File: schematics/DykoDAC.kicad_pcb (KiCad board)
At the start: 2 copper layers, 159.8 x 100.1 mm, 124 parts, among them J1 AC Input, J2 AudioJack3, J3 USB_B, J4 OLED, J5 Debug, J6 Conn_01x02_Male, SW1 PEC09-2120K, U10 TPA6120, U11 IP4234CZ6, U12 ATSAMD21G18A-AUT, U2 L7809, U3 L7909, U4 L7805, U5 78L05, U8 CS4398, U9 AD8620, X1 22.5792Mhz, X2 24.576Mhz

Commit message: pcb dev.
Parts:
- added D3: LED, LEDs:LED_1206, F.Cu at (50.4, -1.77)
- added R39: 680, Resistors_SMD:R_1206, F.Cu at (49.9, 1.39)
- added U6: LP5907-3.3, TO_SOT_Packages_SMD:SOT-23-5, F.Cu at (115.6, 58.2)
- added U7: LP5907-3.3, TO_SOT_Packages_SMD:SOT-23-5, F.Cu at (65.1, 0.81)
- C2, C3: footprint Capacitors_ThroughHole:CP_Radial_D5.0mm_P2.50mm -> kamtar:CP_Radial_D16.0mm_P7.50mm_Hor
- moved U10 186.8 mm to (137.7, 130.9)
- moved U9 183.6 mm to (116.0, 129.3), turned to 270 degrees
- moved U3 160.0 mm to (91.9, 78.1), turned to 180 degrees
- moved U5 154.2 mm to (120.1, 94.7), turned to 180 degrees
- moved U12 149.8 mm to (78.4, 128.0), turned to 180 degrees
- moved C8 149.3 mm to (98.6, 88.5)
- moved U8 146.4 mm to (98.9, 105.3), turned to 180 degrees
- moved R31 137.7 mm to (64.5, 121.0), turned to 180 degrees
- moved U11 136.7 mm to (63.0, 124.6), turned to 90 degrees
- moved R32 132.4 mm to (64.5, 118.6), turned to 180 degrees
- moved U4 126.3 mm to (95.1, 55.0), turned to 180 degrees
- moved C7 124.8 mm to (94.9, 66.2), turned to 90 degrees
- moved C5 122.9 mm to (90.7, 85.7), turned to 180 degrees
- moved C20 119.8 mm to (118.1, 61.5)
- moved C11 118.7 mm to (101.9, 78.1), turned to 90 degrees
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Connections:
- U11 pad 3: (no net) -> /DykoDAC_MCU/USB_D+
- U11 pad 4: Net-(J3-Pad3) -> /DykoDAC_MCU/USB_D-
- U11 pad 6: /DykoDAC_MCU/USB_D- -> Net-(J3-Pad3)
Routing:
- net /DykoDAC_MCU/VBUS_3V3: track 0.00 -> 15.9 mm
- net /DykoDAC_MCU/USB_D-: track 0.00 -> 12.5 mm
- net /DykoDAC_MCU/USB_D+: track 0.00 -> 11.8 mm
- net Net-(J3-Pad1): track 0.00 -> 9.39 mm, vias 0 -> 2
- net VS_NEG: track 0.00 -> 9.18 mm
- net Net-(J3-Pad3): track 0.00 -> 7.38 mm
- net Net-(J3-Pad2): track 0.00 -> 6.13 mm
- net GND: vias 0 -> 54
- added copper zone on F.Cu, net +3V3
- added copper zone on F.Cu, net +9V
- added copper zone on F.Cu, net -9V
- added copper zone on F.Cu, net GND
- added copper zone on F.Cu, net Net-(C14-Pad1)
- added copper zone on F.Cu, net VS_NEG
- removed copper zone on B.Cu, net GND

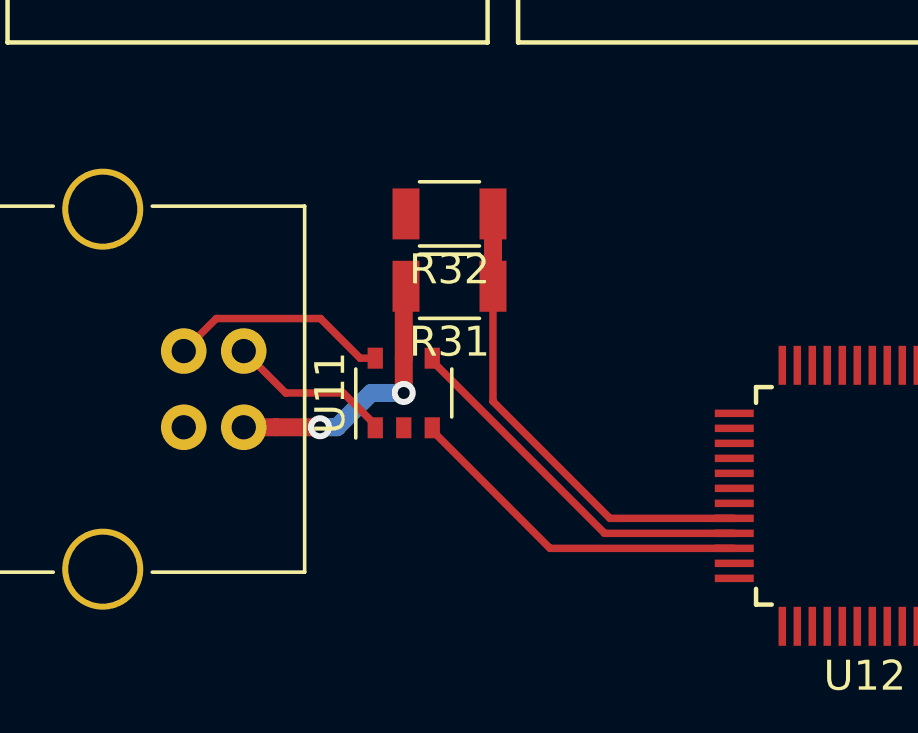
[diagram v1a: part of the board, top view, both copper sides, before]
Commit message: changed usb protection IC
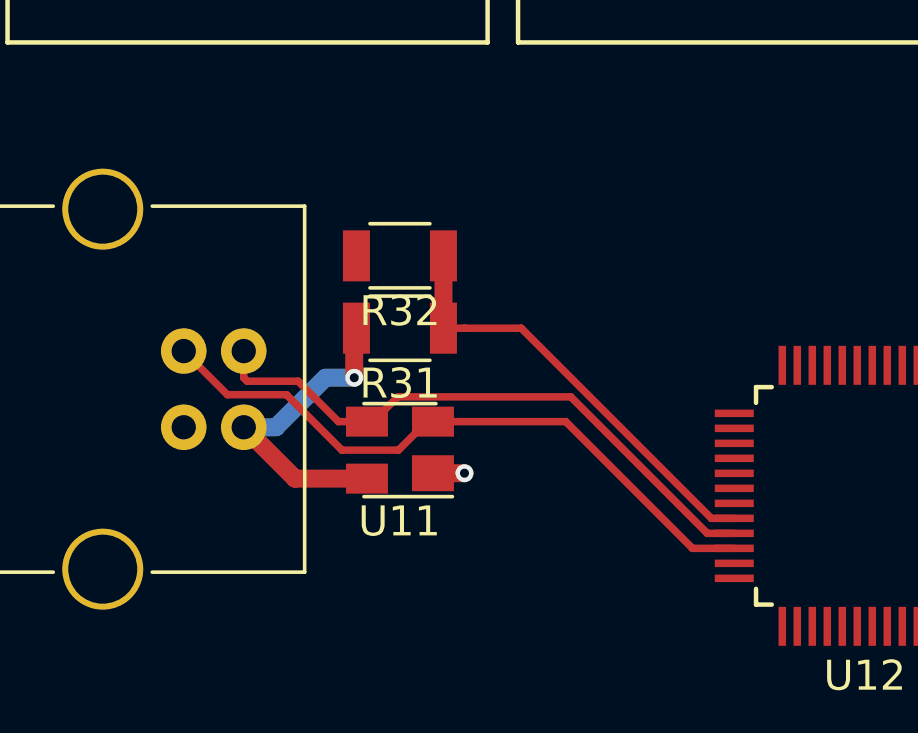
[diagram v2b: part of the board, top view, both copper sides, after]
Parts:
- U11: value IP4234CZ6 -> PRTR5V0U2X.215; footprint Housings_SSOP:TSOP-6_1.65x3.05mm_Pitch0.95mm -> TO_SOT_Packages_SMD:SOT-143
- moved R32 2.16 mm to (62.9, 120.0)
- moved R31 2.16 mm to (62.9, 122.4)
- moved U11 1.91 mm to (62.9, 126.5), turned to 180 degrees
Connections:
- J3 pad 2: Net-(J3-Pad2) -> /DykoDAC_MCU/USB_D-
- J3 pad 3: Net-(J3-Pad3) -> /DykoDAC_MCU/USB_D+
- U11 pad 1: Net-(J3-Pad2) -> GND
- U11 pad 2: GND -> /DykoDAC_MCU/USB_D+
- U11 pad 3: /DykoDAC_MCU/USB_D+ -> /DykoDAC_MCU/USB_D-
- U11 pad 4: /DykoDAC_MCU/USB_D- -> Net-(J3-Pad1)
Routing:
- net /DykoDAC_MCU/USB_D+: track 11.8 -> 21.9 mm
- net /DykoDAC_MCU/USB_D-: track 12.5 -> 21.0 mm
- net Net-(J3-Pad3): track 7.38 -> 0.00 mm
- net Net-(J3-Pad2): track 6.13 -> 0.00 mm
- net Net-(J3-Pad1): track 9.39 -> 10.9 mm, vias 2 -> 1
- net /DykoDAC_MCU/VBUS_3V3: track 15.9 -> 14.7 mm
- net GND: track 0.00 -> 1.05 mm, vias 54 -> 55
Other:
- net class Default: via_dia 0.8 -> 0.6; via_drill 0.4 -> 0.3

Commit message: lots of stuf ....
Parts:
- C30, C31: footprint Capacitors_SMD:C_1206 -> Capacitors_SMD:C_0805
- R35, R36, R37: footprint Resistors_SMD:R_1206 -> Resistors_SMD:R_0603
- R6: footprint Resistors_SMD:R_1206 -> Resistors_SMD:R_0805
- moved C15 161.7 mm to (99.4, 98.7), turned to 90 degrees
- moved X1 159.2 mm to (90.9, 110.7), turned to 270 degrees
- moved X2 155.6 mm to (99.4, 110.9), turned to 270 degrees
- moved C19 154.2 mm to (97.6, 105.7)
- moved R3 149.9 mm to (166.6, 60.2), turned to 90 degrees
- moved C21 146.4 mm to (87.1, 104.5), turned to 90 degrees
- moved C23 144.8 mm to (103.5, 111.0), turned to 270 degrees
- moved C22 143.2 mm to (94.9, 110.9), turned to 270 degrees
- moved L1 141.4 mm to (94.0, 104.1), turned to 270 degrees
- moved C13 138.9 mm to (87.4, 95.8), turned to 270 degrees
- moved R35 136.4 mm to (85.0, 124.7)
- moved C16 136.0 mm to (91.6, 99.8)
- moved R37 129.8 mm to (79.2, 119.4), turned to 90 degrees
- moved R36 124.7 mm to (80.8, 119.4), turned to 90 degrees
- moved U7 106.7 mm to (90.3, 104.5), turned to 180 degrees
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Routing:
- net +3V3: track 0.00 -> 79.4 mm, vias 0 -> 2
- net S_LRCK: track 0.00 -> 10.5 mm
- net S_DOUT: track 0.00 -> 9.80 mm, vias 0 -> 2
- net S_SCLK: track 0.00 -> 8.79 mm
- net Net-(C19-Pad1): track 0.00 -> 8.67 mm
- net VS_POS: track 0.00 -> 6.01 mm, vias 0 -> 2
- net Net-(R36-Pad1): track 0.00 -> 3.81 mm
- net Net-(R37-Pad1): track 0.00 -> 3.69 mm
- net Net-(R35-Pad1): track 0.00 -> 1.80 mm
- net GND: vias 55 -> 1
- added copper zone on F.Cu, net 3V3_OSC
- added copper zone on F.Cu, net Net-(C15-Pad1)

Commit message: no message
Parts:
- added U1: LT1762-5, Housings_SSOP:MSOP-8_3x3mm_Pitch0.65mm, F.Cu at (177.8, 20.6)
- C1, C10, C11, C12, C13, C16, C17, C18, C19, C20, C21, C22, C23, C24, C25, C27, C28, C36, C37, C38, C39, C4, C40, C41, C43, C44, C45, C46, C47, C48, C5, C53, C54, C55, C56, C57, C58, C59, C6, C60, C61, C62, C63: footprint Capacitors_SMD:C_1206 -> Capacitors_SMD:C_0603_HandSoldering
- C26, C29, C33, C34, C35, C42, C50, C52, C9: footprint Capacitors_SMD:C_1206 -> Capacitors_SMD:CP_Elec_4x5.7
- C30, C31: footprint Capacitors_SMD:C_0805 -> Capacitors_SMD:C_0603_HandSoldering
- C32: footprint Capacitors_SMD:C_1206 -> Capacitors_SMD:CP_Elec_6.3x5.8
- D1, D2: footprint Capacitors_SMD:C_1206 -> Diodes_SMD:D_SMB_Handsoldering
- D3: footprint LEDs:LED_1206 -> LEDs:LED_0805_HandSoldering
- R1, R10, R11, R12, R13, R14, R15, R16, R17, R18, R19, R2, R20, R21, R22, R23, R24, R25, R26, R27, R28, R29, R3, R30, R31, R32, R33, R34, R38, R39, R4, R5, R7, R8, R9: footprint Resistors_SMD:R_1206 -> Resistors_SMD:R_0603_HandSoldering
- R35, R36, R37: footprint Resistors_SMD:R_0603 -> Resistors_SMD:R_0603_HandSoldering
- R6: footprint Resistors_SMD:R_0805 -> Resistors_SMD:R_0603_HandSoldering
- moved C1 210.5 mm to (92.6, 178.5)
- moved C24 210.5 mm to (71.4, 191.5)
- moved C36 210.5 mm to (139.3, 172.8)
- moved C37 210.5 mm to (157.5, 156.2)
- moved C38 210.5 mm to (133.7, 175.3)
- moved C39 210.5 mm to (148.5, 163.1)
- moved C40 210.5 mm to (131.6, 172.2)
- moved C41 210.5 mm to (128.2, 175.6)
- moved C43 210.5 mm to (131.6, 169.0)
- moved C44 210.5 mm to (122.6, 175.6)
- moved C45 210.5 mm to (148.5, 169.4)
- moved C46 210.5 mm to (163.0, 156.2)
- moved C47 210.5 mm to (157.5, 159.4)
- moved C49 210.5 mm to (138.8, 147.8)
- moved C50 210.5 mm to (154.1, 163.1)
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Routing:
- net /DykoDAC_MCU/RST: track 0.00 -> 36.4 mm, vias 0 -> 2
- net +3V3: track 79.4 -> 113.0 mm, vias 2 -> 4
- net /DykoDAC_MCU/DBG_RX: track 0.00 -> 15.6 mm
- net /DykoDAC_MCU/DBG_TX: track 0.00 -> 14.7 mm, vias 0 -> 1
- net /DykoDAC_MCU/SWCLK: track 0.00 -> 14.4 mm
- net /DykoDAC_MCU/SWDIO: track 0.00 -> 13.2 mm, vias 0 -> 1
- net S_DOUT: track 9.80 -> 0.00 mm, vias 2 -> 0
- net 3V3_OSC: track 0.00 -> 8.87 mm
- net S_LRCK: track 10.5 -> 3.14 mm
- net S_SCLK: track 8.79 -> 1.42 mm
- net GND: track 1.05 -> 3.63 mm, vias 1 -> 2

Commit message: opamp filter pcb
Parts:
- removed J6: Conn_01x02_Male, Pin_Headers:Pin_Header_Straight_1x02_Pitch2.54mm
- removed L2: 100u, Choke_SMD:Choke_SMD_1206_Standard
- added C64: 10u, Capacitors_Tantalum_SMD:CP_Tantalum_Case-A_EIA-3216-18_Reflow, F.Cu at (14.2, 90.1)
- added C65: 10u, Capacitors_Tantalum_SMD:CP_Tantalum_Case-A_EIA-3216-18_Reflow, F.Cu at (14.2, 93.6)
- added C66: 0.1u, Capacitors_SMD:C_0603, F.Cu at (21.4, 57.2)
- added Q1: MMBT3904, TO_SOT_Packages_SMD:SOT-23, F.Cu at (17.3, 58.3)
- added R40: 240, Resistors_SMD:R_0603, F.Cu at (19.3, 89.6)
- added R41: 1k5, Resistors_SMD:R_0603, F.Cu at (19.3, 92.1)
- added R42: 1k5, Resistors_SMD:R_0603, F.Cu at (9.47, 57.3)
- added R43: 240, Resistors_SMD:R_0603, F.Cu at (19.3, 94.6)
- added R44: 50, Resistors_SMD:R_0603, F.Cu at (9.23, 104.1)
- added R45: 10k, Resistors_SMD:R_0603, F.Cu at (25.1, 57.3)
- C1, C10, C11, C12, C13, C16, C17, C18, C20, C21, C24, C25, C27, C28, C30, C31, C36, C37, C38, C39, C4, C40, C41, C43, C44, C45, C46, C47, C48, C5, C53, C54, C55, C56, C57, C58, C6, C60, C61, C62, C63: footprint Capacitors_SMD:C_0603_HandSoldering -> Capacitors_SMD:C_0603
- C14, C15: value 470u -> 10u; footprint Capacitors_SMD:CP_Elec_8x6.7 -> Capacitors_Tantalum_SMD:CP_Tantalum_Case-A_EIA-3216-18_Reflow
- C19: value 22u -> 1u; footprint Capacitors_SMD:C_0603_HandSoldering -> Capacitors_SMD:C_0603
- C22, C23: value 100n -> 0.1u; footprint Capacitors_SMD:C_0603_HandSoldering -> Capacitors_SMD:C_0603
- C26, C29, C33, C35, C42, C50, C52, C9: footprint Capacitors_SMD:CP_Elec_4x5.7 -> Capacitors_Tantalum_SMD:CP_Tantalum_Case-A_EIA-3216-18_Reflow
- C32: footprint Capacitors_SMD:CP_Elec_6.3x5.8 -> Capacitors_Tantalum_SMD:CP_Tantalum_Case-D_EIA-7343-31_Reflow
- C34: footprint Capacitors_SMD:CP_Elec_4x5.7 -> Capacitors_Tantalum_SMD:CP_Tantalum_Case-B_EIA-3528-21_Reflow
- C49, C51: footprint Capacitors_SMD:CP_Elec_5x4.5 -> Capacitors_Tantalum_SMD:CP_Tantalum_Case-D_EIA-7343-31_Reflow
- C59: value 1u -> 10u; footprint Capacitors_SMD:C_0603_HandSoldering -> Capacitors_Tantalum_SMD:CP_Tantalum_Case-A_EIA-3216-18_Reflow
- C7, C8: value 470u -> 100u; footprint Capacitors_SMD:CP_Elec_8x6.7 -> Capacitors_Tantalum_SMD:CP_Tantalum_Case-D_EIA-7343-31_Reflow
- D1, D2: footprint Diodes_SMD:D_SMB_Handsoldering -> Diodes_SMD:D_SMB
- D3: footprint LEDs:LED_0805_HandSoldering -> LEDs:LED_D3.0mm
- J2: value AudioJack3 -> AudioJack2_Ground_Switch; footprint Connect:JACK_ALIM -> Connect:Stereo_Jack_3.5mm_Switch_Ledino_KB3SPRS
- J5: footprint Pin_Headers:Pin_Header_Straight_2x04_Pitch2.54mm -> Pin_Headers:Pin_Header_Angled_2x03_Pitch1.27mm
- L1: value 100u -> Ferrite Bead; footprint Choke_SMD:Choke_SMD_1206_Standard -> Capacitors_SMD:C_0603
- R1, R10, R11, R12, R13, R14, R15, R16, R17, R18, R19, R2, R20, R21, R22, R23, R24, R25, R26, R27, R28, R29, R3, R30, R31, R32, R33, R34, R35, R36, R37, R38, R4, R5, R6, R7, R8, R9: footprint Resistors_SMD:R_0603_HandSoldering -> Resistors_SMD:R_0603
- R39: value 680 -> 240; footprint Resistors_SMD:R_0603_HandSoldering -> Resistors_SMD:R_0603
- SW1: footprint Pin_Headers:Pin_Header_Angled_1x05_Pitch2.54mm -> Potentiometers:Potentiometer_Alps_RK097_Double_Vertical
- U10: value TPA6120 -> TPA6120A2; footprint Housings_SOIC:HSOP-20-1EP_11.0x15.9mm_Pitch1.27mm_SlugDown -> test:SOIC-20W_ThermalPad
- U2: value L7809 -> LM317; footprint TO_SOT_Packages_SMD:TO-263-2 -> TO_SOT_Packages_SMD:SOT-223-3_TabPin2
- U3: value L7909 -> LM337; footprint TO_SOT_Packages_SMD:TO-263-2 -> TO_SOT_Packages_SMD:SOT-223-3_TabPin2
- U4: footprint TO_SOT_Packages_SMD:TO-263-2 -> TO_SOT_Packages_SMD:SOT-223-3_TabPin2
- U5: footprint TO_SOT_Packages_SMD:SOT-89-3 -> TO_SOT_Packages_SMD:SOT-23
- X1, X2: footprint Oscillators:Oscillator_SMD_TXC_7C-4pin_5.0x3.2mm_HandSoldering -> Oscillators:Oscillator_SMD_Abracon_ASE-4pin_3.2x2.5mm
- moved R39 171.8 mm to (19.2, 52.8)
- moved R21 166.8 mm to (3.98, 113.0)
- moved C53 166.8 mm to (4.08, 109.8)
- moved R26 160.9 mm to (34.7, 68.1)
- moved R27 160.9 mm to (35.4, 100.6)
- moved C47 160.9 mm to (27.3, 64.8)
- moved C50 160.9 mm to (23.9, 68.5)
- moved C52 160.9 mm to (18.3, 71.7)
- moved C54 160.9 mm to (14.6, 78.2)
- moved C55 160.9 mm to (36.0, 89.0)
- moved C56 160.9 mm to (24.4, 100.6)
- moved C57 160.9 mm to (18.2, 103.8)
- moved C58 160.9 mm to (23.8, 103.8)
- moved C59 160.9 mm to (18.2, 107.0)
- moved C61 160.9 mm to (18.2, 110.2)
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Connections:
- C62 pad 2: Net-(C62-Pad2) -> +3V3
- C63 pad 1: Net-(C63-Pad1) -> GND
- C63 pad 2: GND -> Net-(C63-Pad2)
- D3 pad 1: GND -> Net-(D3-Pad1)
- J2 pad 1: (no net) -> GND
- J2 pad 2: (no net) -> Net-(J2-Pad2)
- J2 pad 3: (no net) -> Net-(J2-Pad3)
- J5 pad 1: +3V3 -> GND
- R25 pad 1: Net-(J2-PadT) -> Net-(J2-Pad3)
- R26 pad 1: Net-(J2-PadR) -> Net-(J2-Pad2)
- R39 pad 1: /DykoDAC_MCU/LED_TEST -> +3V3
- U1 pad 6: Net-(U1-Pad6) -> (no net)
- U1 pad 7: Net-(U1-Pad7) -> (no net)
- U12 pad 1: Net-(U12-Pad1) -> (no net)
- U12 pad 10: Net-(U12-Pad10) -> (no net)
- U12 pad 11: Net-(U12-Pad11) -> (no net)
- U12 pad 13: Net-(U12-Pad13) -> (no net)
- U12 pad 2: Net-(U12-Pad2) -> (no net)
- U12 pad 20: Net-(U12-Pad20) -> (no net)
- U12 pad 3: Net-(U12-Pad3) -> (no net)
- U12 pad 30: Net-(U12-Pad30) -> (no net)
- U12 pad 31: Net-(U12-Pad31) -> (no net)
- U12 pad 37: Net-(U12-Pad37) -> (no net)
- U12 pad 38: Net-(U12-Pad38) -> (no net)
- U12 pad 39: Net-(U12-Pad39) -> (no net)
- U12 pad 4: Net-(U12-Pad4) -> (no net)
- U12 pad 41: Net-(U12-Pad41) -> (no net)
- U12 pad 43: Net-(C63-Pad1) -> Net-(C63-Pad2)
- U12 pad 6: Net-(C62-Pad2) -> +3V3
- U2 pad 1: VS_POS -> Net-(C64-Pad1)
- U2 pad 2: GND -> VS_POS
- U3 pad 1: GND -> Net-(C65-Pad2)
- U6 pad 4: Net-(U6-Pad4) -> (no net)
- U7 pad 4: Net-(U7-Pad4) -> (no net)
- U8 pad 18: Net-(U8-Pad18) -> (no net)
- U8 pad 25: Net-(U8-Pad25) -> (no net)
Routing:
- net +3V3: track 113.0 -> 0.00 mm, vias 4 -> 0
- net /DykoDAC_MCU/RST: track 36.4 -> 0.00 mm, vias 2 -> 0
- net AOUTB+: track 0.00 -> 32.6 mm
- net AOUTB-: track 0.00 -> 24.1 mm
- net /DykoDAC_MCU/USB_D+: track 21.9 -> 0.00 mm
- net /DykoDAC_MCU/USB_D-: track 21.0 -> 0.00 mm
- net /DykoDAC_MCU/DBG_RX: track 15.6 -> 0.00 mm
- net Net-(R19-Pad1): track 0.00 -> 14.8 mm
- net /DykoDAC_MCU/VBUS_3V3: track 14.7 -> 0.00 mm
- net /DykoDAC_MCU/DBG_TX: track 14.7 -> 0.00 mm, vias 1 -> 0
- net /DykoDAC_MCU/SWCLK: track 14.4 -> 0.00 mm
- net /DykoDAC_MCU/SWDIO: track 13.2 -> 0.00 mm, vias 1 -> 0
- net Net-(J3-Pad1): track 10.9 -> 0.00 mm, vias 1 -> 0
- net VS_NEG: track 9.18 -> 0.00 mm
- net 3V3_OSC: track 8.87 -> 0.00 mm
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- added copper zone on F.Cu, net Net-(C37-Pad1)
- added copper zone on F.Cu, net Net-(C38-Pad1)
- added copper zone on F.Cu, net Net-(C41-Pad1)
- removed copper zone on F.Cu, net +3V3
- removed copper zone on F.Cu, net 3V3_OSC
- removed copper zone on F.Cu, net Net-(C14-Pad1)
- removed copper zone on F.Cu, net Net-(C15-Pad1)
- removed copper zone on F.Cu, net Net-(D1-Pad2)
- removed copper zone on F.Cu, net Net-(F1-Pad2)
- removed copper zone on F.Cu, net VS_NEG
- removed copper zone on F.Cu, net VS_POS
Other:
- board text added: "AudioJack"
- board text added: "ENCODER"
- board text added: "LED Indicator"
- board text added: "OLED"
- board text added: "POWER JACK"
- board text added: "USB B"

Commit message: pcb update
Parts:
- added J6: ENC_CONN, Pin_Headers:Pin_Header_Straight_1x04_Pitch1.27mm, F.Cu at (83.9, 122.9)
- added J7: Conn_01x03, Pin_Headers:Pin_Header_Straight_1x03_Pitch1.27mm, F.Cu at (54.5, 156.8)
- added J8: OLED, Pin_Headers:Pin_Header_Straight_1x04_Pitch1.27mm, F.Cu at (50.4, 156.8)
- added J9: Conn_01x03, Pin_Headers:Pin_Header_Straight_1x03_Pitch1.27mm, F.Cu at (58.7, 156.8)
- J5: footprint Pin_Headers:Pin_Header_Angled_2x03_Pitch1.27mm -> Pin_Headers:Pin_Header_Straight_2x03_Pitch2.54mm
- moved C32 116.3 mm to (92.1, 130.8), turned to 180 degrees
- moved C24 91.2 mm to (89.7, 127.5), turned to 180 degrees
- moved R36 66.1 mm to (80.1, 117.9)
- moved R35 64.0 mm to (83.1, 118.7)
- moved R4 58.8 mm to (83.6, 113.9)
- moved C62 57.7 mm to (81.8, 126.0), turned to 90 degrees
- moved C63 56.7 mm to (75.2, 131.1), turned to 270 degrees
- moved R37 55.3 mm to (81.9, 120.5)
- moved U3 55.1 mm to (69.8, 74.3)
- moved R32 49.0 mm to (63.8, 129.7), turned to 180 degrees
- moved C25 41.4 mm to (96.9, 117.1)
- moved C27 40.9 mm to (89.8, 123.4)
- moved C29 38.9 mm to (104.3, 123.1)
- moved C28 37.8 mm to (100.1, 123.3)
- moved C45 37.6 mm to (121.8, 124.8)
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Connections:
- C56 pad 2: /DykoDAC_MCU/ENC_A -> Net-(C56-Pad2)
- C57 pad 1: /DykoDAC_MCU/ENC_B -> Net-(C57-Pad1)
- C58 pad 2: /DykoDAC_MCU/ENC_BUTTON -> /DykoDAC_MCU/BTT
- J4 pad 1: /DykoDAC_MCU/OLED_SDA -> Net-(J4-Pad1)
- J4 pad 2: /DykoDAC_MCU/OLED_SCL -> Net-(J4-Pad2)
- R28 pad 2: /DykoDAC_MCU/ENC_A -> Net-(C56-Pad2)
- R29 pad 1: /DykoDAC_MCU/ENC_B -> Net-(C57-Pad1)
- R30 pad 2: /DykoDAC_MCU/ENC_BUTTON -> /DykoDAC_MCU/BTT
- R33 pad 2: /DykoDAC_MCU/OLED_SCL -> Net-(J4-Pad2)
- R34 pad 2: /DykoDAC_MCU/OLED_SDA -> Net-(J4-Pad1)
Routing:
- net GND: track 6.97 -> 38.9 mm
- net MCU_MOSI: track 0.00 -> 27.8 mm, vias 0 -> 2
- net MCU_MISO: track 0.00 -> 27.4 mm, vias 0 -> 2
- net MCU_SCK: track 0.00 -> 25.2 mm, vias 0 -> 2
- net DAC_CS: track 0.00 -> 25.0 mm, vias 0 -> 2
- net DAC_RST: track 0.00 -> 24.2 mm, vias 0 -> 2
- net Net-(J3-Pad1): track 0.00 -> 23.2 mm
- net +3V3: track 0.00 -> 21.9 mm
- net /DykoDAC_MCU/USB_D+: track 0.00 -> 17.4 mm
- net /DykoDAC_MCU/USB_D-: track 0.00 -> 16.9 mm
- net Net-(R19-Pad1): track 14.8 -> 0.00 mm
- net S_SCLK: track 0.00 -> 13.0 mm
- net +5VA: track 0.00 -> 12.4 mm
- net /DykoDAC_MCU/VBUS_3V3: track 0.00 -> 10.8 mm, vias 0 -> 2
- net S_LRCK: track 0.00 -> 9.73 mm
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
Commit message: pcb
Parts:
- removed C51: 100u, Capacitors_Tantalum_SMD:CP_Tantalum_Case-D_EIA-7343-31_Reflow
- removed Q1: MMBT3904, TO_SOT_Packages_SMD:SOT-23
- removed R44: 50, Resistors_SMD:R_0603
- removed R45: 10k, Resistors_SMD:R_0603
- removed U12: ATSAMD21G18A-AUT, Housings_QFP:TQFP-48_7x7mm_Pitch0.5mm
- added C67: 3.3u, Capacitors_SMD:C_0805, F.Cu at (69.6, 111.6)
- added C68: 0.1u, Capacitors_SMD:C_0603, F.Cu at (70.4, 113.2)
- added L2: Ferrite Bead, Capacitors_SMD:C_0603, F.Cu at (80.1, 103.1)
- added U13: ATSAMD51J20A-A, Housings_QFP:LQFP-64_10x10mm_Pitch0.5mm, F.Cu at (78.2, 115.1)
- C34: footprint Capacitors_Tantalum_SMD:CP_Tantalum_Case-B_EIA-3528-21_Reflow -> Capacitors_SMD:C_0805
- C63: value 1u -> 0.1u
- D3: footprint LEDs:LED_D3.0mm -> LEDs:LED_0603_HandSoldering
- J2: value AudioJack2_Ground_Switch -> AudioJack
- J6: value ENC_CONN -> Conn_01x05; footprint Pin_Headers:Pin_Header_Straight_1x04_Pitch1.27mm -> Pin_Headers:Pin_Header_Straight_1x05_Pitch1.00mm
- J7, J9: value Conn_01x03 -> Conn_01x04; footprint Pin_Headers:Pin_Header_Straight_1x03_Pitch1.27mm -> Pin_Headers:Pin_Header_Straight_1x04_Pitch1.00mm
- J8: value OLED -> Conn_01x05; footprint Pin_Headers:Pin_Header_Straight_1x04_Pitch1.27mm -> Pin_Headers:Pin_Header_Straight_1x05_Pitch1.00mm
- R39: value 240 -> 1k
- moved C54 126.0 mm to (138.3, 102.5), turned to 180 degrees
- moved C1 125.7 mm to (113.9, 116.6), turned to 270 degrees
- moved R22 122.5 mm to (138.4, 109.9)
- moved R23 121.5 mm to (138.4, 108.3), turned to 180 degrees
- moved C48 119.6 mm to (138.3, 106.0)
- moved C53 119.4 mm to (123.3, 103.1)
- moved R21 119.0 mm to (122.9, 110.0), turned to 180 degrees
- moved R26 109.6 mm to (138.2, 104.3), turned to 180 degrees
- moved C52 109.1 mm to (123.8, 99.4)
- moved R42 103.4 mm to (106.2, 93.7)
- moved C47 103.3 mm to (121.8, 106.4), turned to 180 degrees
- moved C50 101.1 mm to (118.5, 104.1), turned to 270 degrees
- moved R24 100.7 mm to (122.9, 108.5)
- moved R39 97.9 mm to (82.0, 127.9), turned to 90 degrees
- moved R25 97.1 mm to (123.3, 104.6)
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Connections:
- C49 pad 1: +9V -> +3V3
- C59 pad 1: +3V3 -> /DykoDAC_MCU/VDD_F
- C60 pad 2: +3V3 -> /DykoDAC_MCU/VDD_F
- C61 pad 2: +3V3 -> /DykoDAC_MCU/VDD_F
- C62 pad 2: +3V3 -> Net-(C62-Pad2)
- C63 pad 2: Net-(C63-Pad2) -> /DykoDAC_MCU/VDD_F
- D3 pad 1: Net-(D3-Pad1) -> /DykoDAC_MCU/LED_TEST
- J4 pad 3: +3V3 -> /DykoDAC_MCU/3V3_Oled
- J6 pad 1: /DykoDAC_MCU/ENC_BUTTON -> +3V3
- J6 pad 2: /DykoDAC_MCU/ENC_B -> /DykoDAC_MCU/ENC_A
- J6 pad 3: /DykoDAC_MCU/ENC_A -> /DykoDAC_MCU/ENC_B
- J6 pad 4: +3V3 -> /DykoDAC_MCU/ENC_BUTTON
- J7 pad 1: /DykoDAC_MCU/OLED_SDA -> +3V3
- J7 pad 2: /DykoDAC_MCU/OLED_SCL -> /DykoDAC_MCU/OLED_SDA
- J7 pad 3: GND -> /DykoDAC_MCU/OLED_SCL
- J8 pad 1: /DykoDAC_MCU/BTT -> /DykoDAC_MCU/3V3_Conn
- J8 pad 2: Net-(C57-Pad1) -> Net-(C56-Pad2)
- J8 pad 3: Net-(C56-Pad2) -> Net-(C57-Pad1)
- J8 pad 4: +3V3 -> /DykoDAC_MCU/BTT
- J9 pad 1: Net-(J4-Pad1) -> /DykoDAC_MCU/3V3_Oled
- J9 pad 2: Net-(J4-Pad2) -> Net-(J4-Pad1)
- J9 pad 3: GND -> Net-(J4-Pad2)
- R28 pad 1: +3V3 -> /DykoDAC_MCU/3V3_Conn
- R29 pad 2: +3V3 -> /DykoDAC_MCU/3V3_Conn
- R30 pad 1: +3V3 -> /DykoDAC_MCU/3V3_Conn
- R33 pad 1: +3V3 -> /DykoDAC_MCU/3V3_Oled
- R34 pad 1: +3V3 -> /DykoDAC_MCU/3V3_Oled
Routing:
- net +3V3: track 21.9 -> 187.6 mm, vias 0 -> 5
- net +9V: track 4.85 -> 102.6 mm, vias 0 -> 4
- net -9V: track 4.68 -> 81.2 mm, vias 0 -> 2
- net VS_NEG: track 0.00 -> 75.1 mm
- net VS_POS: track 0.00 -> 68.1 mm
- net GND: track 38.9 -> 100.0 mm, vias 0 -> 66
- net Net-(J2-Pad3): track 0.00 -> 30.1 mm, vias 0 -> 2
- net /DykoDAC_MCU/VDD_F: track 0.00 -> 26.1 mm
- net Net-(R20-Pad1): track 2.02 -> 24.6 mm
- net /DykoDAC_MCU/RST: track 6.15 -> 28.0 mm, vias 0 -> 4
- net Net-(D1-Pad2): track 0.00 -> 21.2 mm
- net +5VA: track 12.4 -> 30.4 mm, vias 0 -> 2
- net OSC_EN_2: track 0.00 -> 17.0 mm, vias 0 -> 2
- net Net-(R19-Pad1): track 0.00 -> 16.0 mm
- net /DykoDAC_MCU/OLED_SDA: track 0.00 -> 15.7 mm
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- added copper zone on F.Cu, net +3V3
- added copper zone on F.Cu, net /DykoDAC_MCU/VDD_F
- added copper zone on B.Cu, net GND
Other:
- board text removed: "LED Indicator"
